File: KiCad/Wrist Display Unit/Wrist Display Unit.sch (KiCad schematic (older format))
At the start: 20 parts, among them J1 MICRO_USB, U1 MCP73831

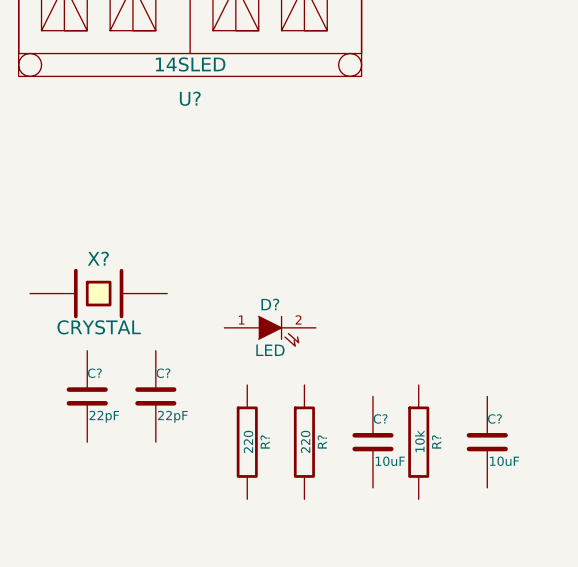
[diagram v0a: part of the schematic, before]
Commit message: Updated Components - 2:45 AM
Nearly all of the weapon components delegated
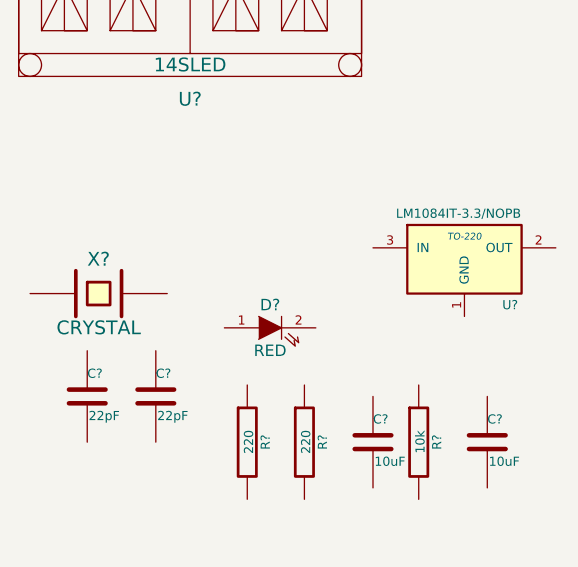
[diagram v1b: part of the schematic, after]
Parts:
- added U?: LM1084IT-3.3/NOPB, TO-220, symbol LM1084IT-3.3/NOPB
- D?: value LED -> RED
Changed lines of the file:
@@
 P 8350 3700
 F 0 "D?" H 8350 3800 50  0000 C CNN
-F 1 "LED" H 8350 3600 50  0000 C CNN
+F 1 "RED" H 8350 3600 50  0000 C CNN
 F 2 "~" H 8350 3700 60  0000 C CNN
 F 3 "~" H 8350 3700 60  0000 C CNN
@@
 	1    0    0    -1
 $EndComp
+$Comp
+L LM1084IT-3.3/NOPB U?
+U 1 1 5501240B
+P 9200 3400
+F 0 "U?" H 9400 3200 40  0000 C CNN
+F 1 "LM1084IT-3.3/NOPB" H 8900 3600 40  0000 L CNN
+F 2 "TO-220" H 9200 3500 30  0000 C CIN
+F 3 "~" H 9200 3400 60  0000 C CNN
+	1    9200 3400
+	1    0    0    -1
+$EndComp
